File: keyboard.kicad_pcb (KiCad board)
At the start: 2 copper layers, 213 parts, among them IC1 ATMEGA32U4, J1 USBMINI_B05, P1 ISP, P2 GPIO Port, Q1 MOS_P, X1 CRYSTAL

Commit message: ver 0.12
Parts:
- removed C10, C11, C12, C13, C14, C15, C16, C17, C18, C19, C20, C21, C22, C23, C24, C9: 0.1uF, Capacitors_SMD:C_0805
- removed RGBLED13, RGBLED14, RGBLED15, RGBLED16: WS2812B, WS2812B:WS2812B
- added G***: LOGO, cw40-logo:logo, B.Cu at (217.4, 119.1)
- added G***: LOGO, cw40-logo:logo, F.Cu at (217.4, 119.1)
- added MXLED: VAL**, holes:PKRHC, F.Cu at (35.1, 100.8)
- added MXLED: VAL**, holes:PKRHC, F.Cu at (263.1, 99.3)
- added MXLED: VAL**, holes:PKRHC, F.Cu at (99.8, 118.1)
- added MXLED: VAL**, holes:PKRHC, F.Cu at (236.2, 67.6)
- added MXLED: VAL**, holes:PKRHC, F.Cu at (134.4, 83.8)
- J1: moved to F.Cu
- S37: footprint MX1A_alps:MX1ALPS -> 6.25:CHERRY_PCB_625H_Rev
- moved P2 155.2 mm to (261.1, 72.1), turned to 270 degrees
- moved LR12 121.5 mm to (38.1, 52.6), turned to 90 degrees
- moved LR10 121.3 mm to (258.8, 52.8), turned to 90 degrees
- moved RGBLED12 111.7 mm to (37.6, 90.2), turned to 270 degrees
- moved RGBLED6 111.7 mm to (258.8, 86.1), turned to 270 degrees
- moved LR23 108.0 mm to (251.7, 71.6), turned to 90 degrees
- moved LR40 106.9 mm to (255.3, 109.5), turned to 90 degrees
- moved C8 106.9 mm to (48.5, 65.5), turned to 180 degrees
- moved R2 106.6 mm to (51.6, 58.9), turned to 90 degrees
- moved D34 106.2 mm to (42.4, 109.2), turned to 270 degrees
- moved LR9 104.5 mm to (240.0, 52.8), turned to 90 degrees
- moved D23 104.3 mm to (45.0, 90.4), turned to 270 degrees
- moved R1 104.3 mm to (54.1, 58.9), turned to 90 degrees
- moved LR11 103.7 mm to (50.0, 70.6), turned to 270 degrees
- moved LR34 102.0 mm to (249.2, 86.9), turned to 90 degrees
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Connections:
- LR35 pad 1: Net-(LR35-Pad1) -> /led/LRow0
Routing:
- net GND: track 0.00 -> 1167.6 mm, vias 0 -> 33
- net VCC: track 0.00 -> 869.7 mm, vias 0 -> 41
- net /led/LRow0: track 0.00 -> 801.4 mm, vias 0 -> 34
- net /Matrix/Row2: track 0.00 -> 314.2 mm, vias 0 -> 2
- net /Matrix/Row3: track 0.00 -> 310.6 mm, vias 0 -> 5
- net /Matrix/Row1: track 0.00 -> 305.8 mm, vias 0 -> 5
- net /led/ESC: track 0.00 -> 293.2 mm, vias 0 -> 3
- net /Matrix/Row0: track 0.00 -> 275.8 mm, vias 0 -> 4
- net /Matrix/Col8: track 0.00 -> 230.9 mm, vias 0 -> 2
- net /Matrix/Col9: track 0.00 -> 227.6 mm, vias 0 -> 2
- net /Matrix/Col10: track 0.00 -> 217.8 mm, vias 0 -> 10
- net /GPIO0: track 0.00 -> 202.2 mm, vias 0 -> 6
- net /GPIO3: track 0.00 -> 167.0 mm, vias 0 -> 3
- net /GPIO2: track 0.00 -> 161.5 mm, vias 0 -> 3
- net /Matrix/Col7: track 0.00 -> 156.4 mm, vias 0 -> 2
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- added copper zone on B.Cu, net (none)
- added copper zone on F.Cu, net (none)
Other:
- board outline added: 229.9 x 77.5 mm
- board text added: "CyptoWall40"
- board text added: "Special Thanks to SmallFry40"

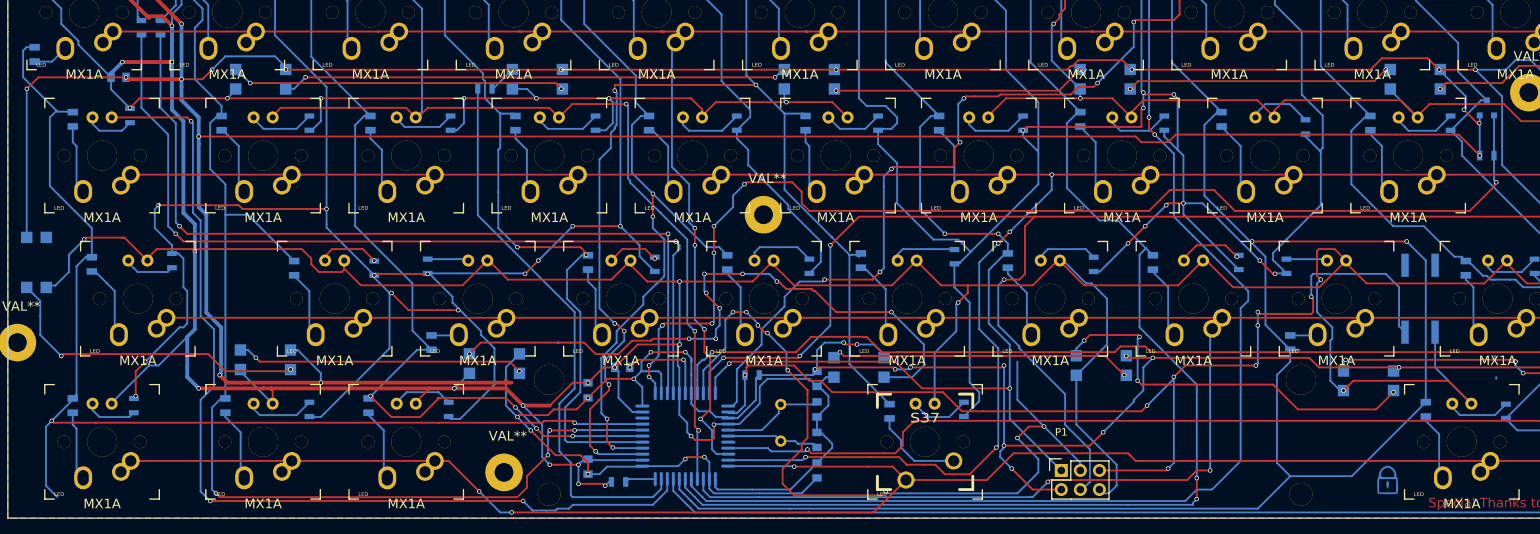
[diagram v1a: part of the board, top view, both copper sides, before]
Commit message: Fix a mistake in underglow
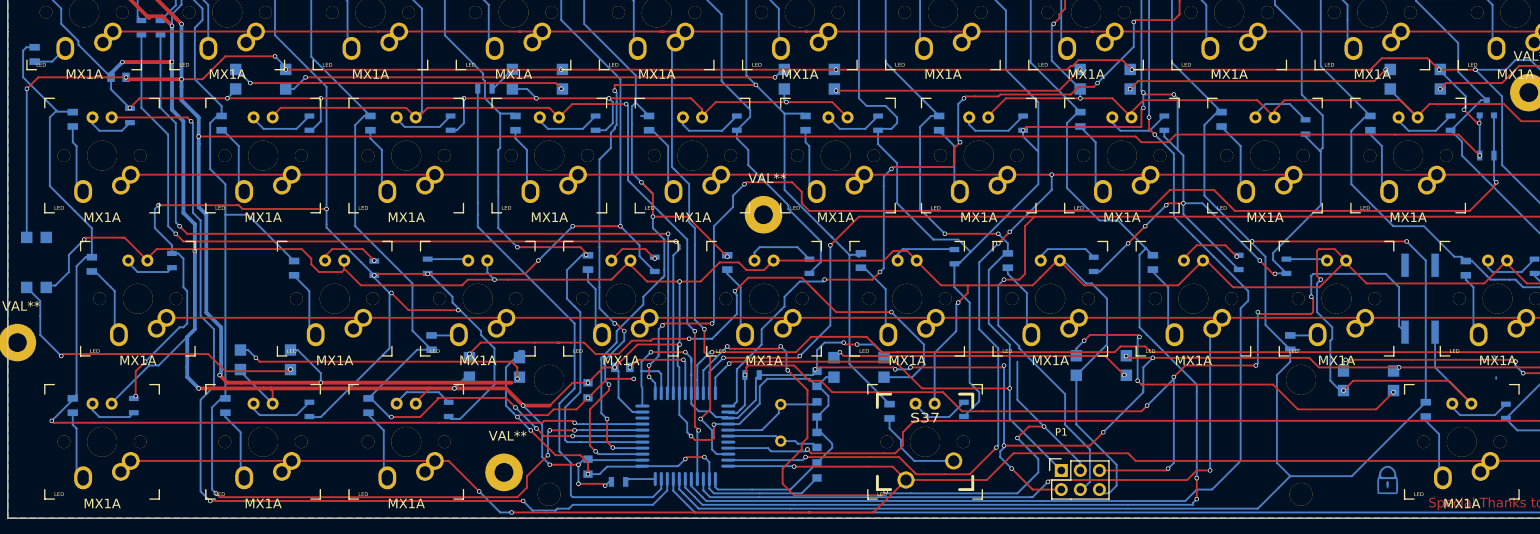
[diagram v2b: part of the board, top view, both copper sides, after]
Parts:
- moved RGBLED10 0.51 mm to (98.6, 104.1)
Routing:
- net /Matrix/Col0: track 150.5 -> 139.4 mm
- net /SCK: track 106.0 -> 100.0 mm, vias 8 -> 6
- net Net-(RGBLED10-Pad4): track 87.0 -> 81.1 mm, vias 9 -> 4
- net /Matrix/Col4: track 94.2 -> 96.8 mm, vias 4 -> 5
- net VCC: track 869.7 -> 868.0 mm
- net Net-(RGBLED10-Pad2): track 38.6 -> 39.7 mm
- net Net-(D27-Pad2): track 9.64 -> 10.5 mm
- net GND: track 1167.6 -> 1168.1 mm, vias 33 -> 34
- net /led/LRow0: vias 34 -> 33
- net /Matrix/Row0: vias 4 -> 2
- net /~Res: vias 8 -> 7
- net /led/Backlight: vias 8 -> 6

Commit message: Slight changes on edge
Gerber files updated also.
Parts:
- moved D20 4.58 mm to (197.9, 67.3)
- moved D27 4.58 mm to (132.1, 86.4)
- moved D28 4.58 mm to (149.9, 86.1)
- moved D29 4.58 mm to (169.4, 86.1)
- moved D30 4.58 mm to (188.7, 86.4)
- moved LED18 4.58 mm to (146.8, 72.1)
- moved LED22 4.58 mm to (222.7, 72.1)
- moved LED5 4.58 mm to (160.8, 53.1)
- moved LR20 4.58 mm to (190.2, 67.8)
- moved LR28 4.58 mm to (143.0, 86.9)
- moved LR29 4.58 mm to (162.3, 85.6)
- moved LR30 4.58 mm to (180.8, 86.6)
- moved LR32 4.58 mm to (206.5, 86.9)
- moved LR7 4.58 mm to (205.0, 49.0)
- moved RGBLED3 4.58 mm to (143.0, 62.0)
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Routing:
- net (no net): track 3.06 -> 0.54 mm
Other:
- outline, holes or cut-outs redrawn

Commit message: a lot of changes
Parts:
- added C10: 100nF, Capacitors_SMD:C_0805, B.Cu at (154.7, 56.4)
- added C11: 100nF, Capacitors_SMD:C_0805, B.Cu at (187.7, 57.9)
- added C12: 100nF, Capacitors_SMD:C_0805, B.Cu at (225.6, 56.4)
- added C13: 100nF, Capacitors_SMD:C_0805, B.Cu at (257.0, 81.8)
- added C14: 100nF, Capacitors_SMD:C_0805, B.Cu at (72.4, 93.7)
- added C15: 100nF, Capacitors_SMD:C_0805, B.Cu at (219.2, 96.5)
- added C16: 100nF, Capacitors_SMD:C_0805, B.Cu at (175.8, 99.3)
- added C17: 100nF, Capacitors_SMD:C_0805, B.Cu at (43.7, 81.8)
- added C18: 100nF, Capacitors_SMD:C_0805, B.Cu at (147.8, 95.5)
- added C19: 100nF, Capacitors_SMD:C_0805, B.Cu at (95.2, 100.3)
- added C9: 100nF, Capacitors_SMD:C_0805, B.Cu at (74.9, 55.9)
- G***, J1: moved to B.Cu
- moved RGBLED2 37.2 mm to (107.2, 62.2)
- moved RGBLED1 36.4 mm to (70.4, 61.7)
- moved LR41 36.4 mm to (63.5, 61.7), turned to 270 degrees
- moved RGBLED3 6.88 mm to (149.9, 61.5)
- moved RGBLED5 5.47 mm to (218.2, 62.2)
- moved RGBLED6 2.55 mm to (261.6, 84.8)
- moved RGBLED7 1.05 mm to (217.7, 101.1)
- moved RGBLED12 0.76 mm to (40.1, 87.1)
- moved RGBLED11 0.57 mm to (70.4, 99.8)
- moved RGBLED8 0.57 mm to (181.6, 100.6)
- moved RGBLED9 0.25 mm to (149.6, 100.6)
- moved RGBLED4 0.25 mm to (182.6, 62.0)
- turned G*** to 180 degrees
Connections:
- IC1 pad 9: /SCK -> /GPIO1
- LR11 pad 1: GND -> VCC
- LR12 pad 1: GND -> VCC
- LR13 pad 1: GND -> VCC
- LR14 pad 1: GND -> VCC
- LR15 pad 1: GND -> VCC
- LR16 pad 1: GND -> VCC
- P1 pad 3: /SCK -> /GPIO1
- P2 pad 4: /GPIO0 -> /GPIO1
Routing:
- net /GPIO1: track 0.00 -> 206.6 mm, vias 0 -> 8
- net VCC: track 868.0 -> 974.4 mm, vias 41 -> 49
- net /SCK: track 100.0 -> 0.00 mm, vias 6 -> 0
- net /GPIO2: track 161.5 -> 227.9 mm, vias 3 -> 6
- net /Matrix/Col10: track 217.8 -> 281.1 mm, vias 10 -> 9
- net GND: track 1168.1 -> 1228.0 mm, vias 34 -> 32
- net /led/Bottom: track 74.8 -> 109.9 mm, vias 0 -> 2
- net Net-(RGBLED2-Pad2): track 67.4 -> 38.0 mm
- net /led/LRow0: track 801.4 -> 818.9 mm, vias 33 -> 32
- net /~Res: track 141.8 -> 128.3 mm, vias 7 -> 3
- net Net-(RGBLED1-Pad2): track 44.6 -> 32.2 mm
- net Net-(RGBLED5-Pad2): track 59.4 -> 66.8 mm
- net Net-(RGBLED3-Pad2): track 34.0 -> 27.3 mm
- net Net-(LR41-Pad1): track 3.77 -> 8.58 mm, vias 0 -> 2
- net Net-(RGBLED4-Pad2): track 35.7 -> 30.9 mm
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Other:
- board text added: "GND"
- board text added: "MISO"
- board text added: "MOSI"
- board text added: "PB0"
- board text added: "PB1"
- board text added: "PB2"
- board text added: "PD1"
- board text added: "RES"
- board text added: "SCK"
- board text added: "USB"
- board text added: "VCC"

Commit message: minor changes & update gerber files
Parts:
- added C20: 100nF, Capacitors_SMD:C_0805, B.Cu at (113.8, 60.7)
- moved RGBLED2 0.25 mm to (107.2, 62.0)
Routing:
- net VCC: track 974.4 -> 978.1 mm
- net GND: track 1228.0 -> 1231.4 mm, vias 32 -> 33
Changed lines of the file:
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@@
 (kicad_pcb (version 4) (host pcbnew 4.0.1-stable)
   (general
-    (links 391)
+    (links 393)
     (no_connects 0)
-    (area 36.246999 42.850999 266.267001 120.471001)
+    (area 21.845069 37.408725 269.727 120.7992)
     (thickness 1.6)
     (drawings 30)
-    (tracks 2701)
+    (tracks 2707)
     (zones 0)
-    (modules 211)
+    (modules 212)
     (nets 135)
   )
@@
     (visible_elements 7FFFFFFF)
     (pcbplotparams
-      (layerselection 0x01800_00000000)
+      (layerselection 0x010ff_80000001)
       (usegerberextensions false)
       (excludeedgelayer true)
@@
       (padsonsilk false)
       (subtractmaskfromsilk false)
-      (outputformat 3)
+      (outputformat 1)
       (mirror false)
       (drillshape 0)
       (scaleselection 1)
-      (outputdirectory C:/Users/Young/Desktop/))
+      (outputdirectory gerber/))
   )
   (net 0 "")
@@
       (effects (font (size 1.27 1.27) (thickness 0.0889)))
     )
-    (fp_text value USBMINI_B05 (at 0 0 360) (layer B.SilkS)
+    (fp_text value USBMINI_B05 (at 0 0 360) (layer B.SilkS) hide
       (effects (font (thickness 0.15)) (justify mirror))
     )
@@
   (module WS2812B:WS2812B (layer B.Cu)
     (at 70.358 61.722 180)
-    (fp_text reference RGBLED1 (at 0 -4 180) (layer B.SilkS)
+    (fp_text reference RGBLED1 (at 0 -4 180) (layer B.SilkS) hide
       (effects (font (size 1 1) (thickness 0.15)) (justify mirror))
     )
@@
   )
   (module WS2812B:WS2812B (layer B.Cu)
-    (at 107.188 62.23 180)
-    (fp_text reference RGBLED2 (at 0 -4 180) (layer B.SilkS)
+    (at 107.188 61.976 180)
+    (fp_text reference RGBLED2 (at 0 -4 180) (layer B.SilkS) hide
       (effects (font (size 1 1) (thickness 0.15)) (justify mirror))
     )
@@
   (module WS2812B:WS2812B (layer B.Cu)
     (at 182.626 61.976 180)
-    (fp_text reference RGBLED4 (at 0 -4 180) (layer B.SilkS)
+    (fp_text reference RGBLED4 (at 0 -4 180) (layer B.SilkS) hide
       (effects (font (size 1 1) (thickness 0.15)) (justify mirror))
     )
@@
   (module WS2812B:WS2812B (layer B.Cu)
     (at 218.186 62.23 180)
-    (fp_text reference RGBLED5 (at 0 -4 180) (layer B.SilkS)
+    (fp_text reference RGBLED5 (at 0 -4 180) (layer B.SilkS) hide
       (effects (font (size 1 1) (thickness 0.15)) (justify mirror))
     )
@@
   (module WS2812B:WS2812B (layer B.Cu)
     (at 261.62 84.836 270)
-    (fp_text reference RGBLED6 (at 0 -4 270) (layer B.SilkS)
+    (fp_text reference RGBLED6 (at 0 -4 270) (layer B.SilkS) hide
       (effects (font (size 1 1) (thickness 0.15)) (justify mirror))
     )
@@
   (module WS2812B:WS2812B (layer B.Cu)
     (at 217.678 101.092 180)
-    (fp_text reference RGBLED7 (at 0.254 3.556 180) (layer B.SilkS)
+    (fp_text reference RGBLED7 (at 0.254 3.556 180) (layer B.SilkS) hide
       (effects (font (size 1 1) (thickness 0.15)) (justify mirror))
     )
@@
   (module WS2812B:WS2812B (layer B.Cu)
     (at 181.61 100.584 180)
-    (fp_text reference RGBLED8 (at 0 -4 180) (layer B.SilkS)
+    (fp_text reference RGBLED8 (at 0 -4 180) (layer B.SilkS) hide
       (effects (font (size 1 1) (thickness 0.15)) (justify mirror))
     )
@@
   (module WS2812B:WS2812B (layer B.Cu)
     (at 149.606 100.584 180)
-    (fp_text reference RGBLED9 (at 0 -4 180) (layer B.SilkS)
+    (fp_text reference RGBLED9 (at 0 -4 180) (layer B.SilkS) hide
       (effects (font (size 1 1) (thickness 0.15)) (justify mirror))
     )
@@
   (module WS2812B:WS2812B (layer B.Cu)
     (at 101.092 100.33 180)
-    (fp_text reference RGBLED10 (at 0 -4 180) (layer B.SilkS)
+    (fp_text reference RGBLED10 (at 0 -4 180) (layer B.SilkS) hide
       (effects (font (size 1 1) (thickness 0.15)) (justify mirror))
     )
@@
   (module WS2812B:WS2812B (layer B.Cu)
     (at 70.358 99.822 180)
-    (fp_text reference RGBLED11 (at 0 -4 180) (layer B.SilkS)
+    (fp_text reference RGBLED11 (at 0 -4 180) (layer B.SilkS) hide
       (effects (font (size 1 1) (thickness 0.15)) (justify mirror))
     )
@@
   (module WS2812B:WS2812B (layer B.Cu)
     (at 40.132 87.122 270)
-    (fp_text reference RGBLED12 (at 0 -4 270) (layer B.SilkS)
+    (fp_text reference RGBLED12 (at 0 -4 270) (layer B.SilkS) hide
       (effects (font (size 1 1) (thickness 0.15)) (justify mirror))
     )
@@
     (tags "capacitor 0805")
     (attr smd)
-    (fp_text reference C12 (at 0 2.1 270) (layer B.SilkS)
+    (fp_text reference C12 (at 0 -1.778 270) (layer B.SilkS)
       (effects (font (size 1 1) (thickness 0.15)) (justify mirror))
     )
@@
     (tags "capacitor 0805")
     (attr smd)
-    (fp_text reference C15 (at 0 2.1 270) (layer B.SilkS)
+    (fp_text reference C15 (at 0 -1.778 270) (layer B.SilkS)
       (effects (font (size 1 1) (thickness 0.15)) (justify mirror))
     )
@@
     (tags "capacitor 0805")
     (attr smd)
-    (fp_text reference C16 (at 0 2.1 90) (layer B.SilkS)
+    (fp_text reference C16 (at 0 -1.524 90) (layer B.SilkS)
       (effects (font (size 1 1) (thickness 0.15)) (justify mirror))
     )
@@
     (tags "capacitor 0805")
     (attr smd)
-    (fp_text reference C19 (at 0 2.1 90) (layer B.SilkS)
+    (fp_text reference C19 (at 0 -1.778 90) (layer B.SilkS)
+      (effects (font (size 1 1) (thickness 0.15)) (justify mirror))
+    )
+    (fp_text value 100nF (at 0 -2.1 90) (layer B.Fab)
+      (effects (font (size 1 1) (thickness 0.15)) (justify mirror))
+    )
+    (fp_line (start -1.8 1) (end 1.8 1) (layer B.CrtYd) (width 0.05))
+    (fp_line (start -1.8 -1) (end 1.8 -1) (layer B.CrtYd) (width 0.05))
+    (fp_line (start -1.8 1) (end -1.8 -1) (layer B.CrtYd) (width 0.05))
+    (fp_line (start 1.8 1) (end 1.8 -1) (layer B.CrtYd) (width 0.05))
+    (fp_line (start 0.5 0.85) (end -0.5 0.85) (layer B.SilkS) (width 0.15))
+    (fp_line (start -0.5 -0.85) (end 0.5 -0.85) (layer B.SilkS) (width 0.15))
+    (pad 1 smd rect (at -1 0 90) (size 1 1.25) (layers B.Cu B.Paste B.Mask)
+      (net 2 GND))
+    (pad 2 smd rect (at 1 0 90) (size 1 1.25) (layers B.Cu B.Paste B.Mask)
+      (net 5 VCC))
+    (model Capacitors_SMD.3dshapes/C_0805.wrl
+      (at (xyz 0 0 0))
+      (scale (xyz 1 1 1))
+      (rotate (xyz 0 0 0))
+    )
+  )
+  (module Capacitors_SMD:C_0805 (layer B.Cu)
+    (at 113.792 60.706 90)
+    (descr "Capacitor SMD 0805, reflow soldering, AVX (see smccp.pdf)")
+    (tags "capacitor 0805")
+    (attr smd)
+    (fp_text reference C20 (at 0 2.1 90) (layer B.SilkS)
       (effects (font (size 1 1) (thickness 0.15)) (justify mirror))
     )
@@
   (segment (start 138.938 106.426) (end 138.43 106.934) (width 0.25) (layer B.Cu) (net 1))
   (segment (start 138.938 105.50906) (end 139.192 105.25506) (width 0.25) (layer B.Cu) (net 1))
+  (segment (start 113.792 61.706) (end 113.792 63.246) (width 0.25) (layer B.Cu) (net 2))
+  (via (at 115.062 64.516) (size 0.6) (drill 0.4) (layers F.Cu B.Cu) (net 2))
+  (segment (start 113.792 63.246) (end 115.062 64.516) (width 0.25) (layer B.Cu) (net 2))
   (segment (start 165.608 69.088) (end 156.521998 69.088) (width 0.25) (layer F.Cu) (net 2))
   (segment (start 166.81577 67.88023) (end 165.608 69.088) (width 0.25) (layer F.Cu) (net 2))
@@
   (segment (start 97.028 64.516) (end 77.978 64.516) (width 0.25) (layer F.Cu) (net 2))
   (segment (start 106.68 64.516) (end 97.028 64.516) (width 0.25) (layer F.Cu) (net 2))
-  (segment (start 116.332 64.516) (end 106.68 64.516) (width 0.25) (layer F.Cu) (net 2))
+  (segment (start 116.332 64.516) (end 115.062 64.516) (width 0.25) (layer F.Cu) (net 2))
+  (segment (start 115.062 64.516) (end 106.68 64.516) (width 0.25) (layer F.Cu) (net 2))
   (segment (start 116.84 64.516) (end 116.332 64.516) (width 0.25) (layer F.Cu) (net 2))
   (segment (start 143.526 110.49) (end 141.478 110.49) (width 0.25) (layer B.Cu) (net 3))
@@
   (via (at 119.126 100.33) (size 0.6) (drill 0.4) (layers F.Cu B.Cu) (net 4))
   (segment (start 120.142 99.314) (end 119.126 100.33) (width 0.25) (layer F.Cu) (net 4))
+  (segment (start 113.792 59.706) (end 111.488 59.706) (width 0.25) (layer B.Cu) (net 5))
+  (segment (start 111.488 59.706) (end 110.518 60.676) (width 0.25) (layer B.Cu) (net 5))
   (segment (start 148.844 57.658) (end 146.812 57.658) (width 0.25) (layer F.Cu) (net 5))
   (segment (start 154.686 57.388) (end 154.416 57.658) (width 0.25) (layer F.Cu) (net 5))

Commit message: final version
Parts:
- turned D25 to 270 degrees
- turned D31 to 270 degrees
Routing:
- net /~Res: track 128.3 -> 119.4 mm
- net /Matrix/Col8: track 230.9 -> 235.0 mm
- net Net-(D25-Pad2): track 3.68 -> 4.61 mm
- net Net-(D31-Pad2): track 3.68 -> 4.61 mm
- net /Matrix/Col2: track 113.5 -> 114.1 mm
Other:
- board text added: "Rev Final"
